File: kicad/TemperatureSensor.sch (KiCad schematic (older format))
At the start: 0 parts

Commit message: First draft of some of the sub-sheets
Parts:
- added R? (x3): 0Ω, symbol Device:R
- added U?: DS7505S, symbol FieldDevice_R2:DS7505S
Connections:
- new net: R?.1, U?.5 (A2)
- new net: R?.1, U?.6 (A1)
- new net: R?.1, U?.7 (A0)
- new net GND: R?.2, R?.2, R?.2, U?.4 (GND)
- new net O.S.: U?.3 (O.S.)
- new net SCL_TEMP: U?.2 (SCL)
- new net SDA: U?.1 (SDA)
- new net Vbb: U?.8 (VDD)
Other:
- note added: "Slave address is \n1 0 0 1 A2 A1 A0"
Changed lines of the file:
@@
 EESchema Schematic File Version 4
 LIBS:FieldDevice_R2-cache
+LIBS:FieldDevice_Power_5V-cache
 EELAYER 26 0
 EELAYER END
 $Descr A4 11693 8268
 encoding utf-8
-Sheet 1 8
+Sheet 4 8
 Title ""
 Date ""
@@
 Comment4 ""
 $EndDescr
+$Comp
+L FieldDevice_R2:DS7505S U?
+U 1 1 5C6AF879
+P 5750 3300
+F 0 "U?" H 6100 2950 50  0000 C CNN
+F 1 "DS7505S" H 5750 3300 50  0000 C CNN
+F 2 "" H 5800 3300 50  0001 C CNN
+F 3 "" H 5800 3300 50  0001 C CNN
+	1    5750 3300
+	1    0    0    -1
+$EndComp
+$Comp
+L FieldDevice_Power_5V-rescue:GND #PWR?
+U 1 1 5C6AF900
+P 5750 4100
+F 0 "#PWR?" H 5750 3850 50  0001 C CNN
+F 1 "GND" H 5755 3927 50  0000 C CNN
+F 2 "" H 5750 4100 50  0001 C CNN
+F 3 "" H 5750 4100 50  0001 C CNN
+	1    5750 4100
+	1    0    0    -1
+$EndComp
+Wire Wire Line
+	5750 3800 5750 4100
+$Comp
+L Device:R R?
+U 1 1 5C6AF92E
+P 6450 3650
+F 0 "R?" H 6520 3696 50  0000 L CNN
+F 1 "0Ω" H 6520 3605 50  0000 L CNN
+F 2 "" V 6380 3650 50  0001 C CNN
+F 3 "~" H 6450 3650 50  0001 C CNN
+	1    6450 3650
+	1    0    0    -1
+$EndComp
+$Comp
+L Device:R R?
+U 1 1 5C6AF9A1
+P 6700 3650
+F 0 "R?" H 6770 3696 50  0000 L CNN
+F 1 "0Ω" H 6770 3605 50  0000 L CNN
+F 2 "" V 6630 3650 50  0001 C CNN
+F 3 "~" H 6700 3650 50  0001 C CNN
+	1    6700 3650
+	1    0    0    -1
+$EndComp
+$Comp
+L Device:R R?
+U 1 1 5C6AF9C3
+P 6950 3650
+F 0 "R?" H 7020 3696 50  0000 L CNN
+F 1 "0Ω" H 7020 3605 50  0000 L CNN
+F 2 "" V 6880 3650 50  0001 C CNN
+F 3 "~" H 6950 3650 50  0001 C CNN
+	1    6950 3650
+	1    0    0    -1
+$EndComp
+Wire Wire Line
+	6350 3450 6450 3450
+Wire Wire Line
+	6450 3450 6450 3500
+Wire Wire Line
+	6350 3350 6700 3350
+Wire Wire Line
+	6700 3350 6700 3500
+Wire Wire Line
+	6350 3250 6950 3250
+Wire Wire Line
+	6950 3250 6950 3500
+$Comp
+L FieldDevice_Power_5V-rescue:GND #PWR?
+U 1 1 5C6AFAFC
+P 7050 4050
+F 0 "#PWR?" H 7050 3800 50  0001 C CNN
+F 1 "GND" H 7055 3877 50  0000 C CNN
+F 2 "" H 7050 4050 50  0001 C CNN
+F 3 "" H 7050 4050 50  0001 C CNN
+	1    7050 4050
+	1    0    0    -1
+$EndComp
+Text Notes 7050 3400 0    50   ~ 0
+Slave address is \n1 0 0 1 A2 A1 A0
+Wire Wire Line
+	6450 3800 6450 3950
+Wire Wire Line
+	6450 3950 6700 3950
+Wire Wire Line
+	7050 3950 7050 4050
+Wire Wire Line
+	6950 3800 6950 3950
+Connection ~ 6950 3950
+Wire Wire Line
+	6950 3950 7050 3950
+Wire Wire Line
+	6700 3800 6700 3950
+Connection ~ 6700 3950
+Wire Wire Line
+	6700 3950 6950 3950
+Wire Wire Line
+	5150 3100 4900 3100
+Wire Wire Line
+	5150 3200 4900 3200
+Wire Wire Line
+	5150 3450 4900 3450
+Text HLabel 4900 3450 0    50   Input ~ 0
+O.S.
+Text HLabel 4900 3200 0    50   Input ~ 0
+SCL_TEMP
+Text HLabel 4900 3100 0    50   Input ~ 0
+SDA
+Wire Wire Line
+	5750 2800 5750 2650
+Wire Wire Line
+	5750 2650 4900 2650
+Text HLabel 4900 2650 0    50   Input ~ 0
+Vbb
 $EndSCHEMATC

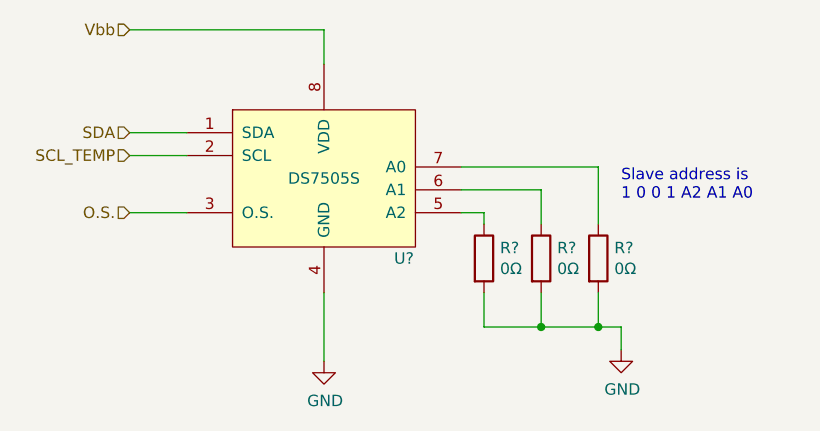
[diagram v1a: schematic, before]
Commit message: Added some more detail and moved the display from SPI to I2C
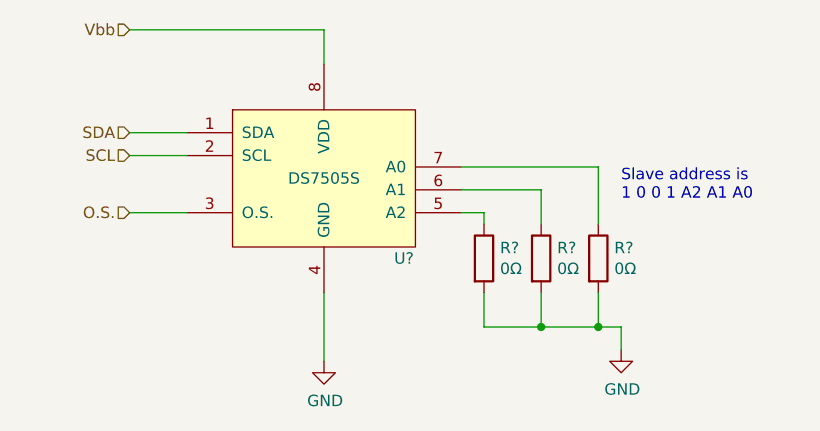
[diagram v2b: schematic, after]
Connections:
- net SCL_TEMP renamed SCL
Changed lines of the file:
@@
 EESchema Schematic File Version 4
 LIBS:FieldDevice_R2-cache
-LIBS:FieldDevice_Power_5V-cache
-EELAYER 26 0
+EELAYER 29 0
 EELAYER END
 $Descr A4 11693 8268
@@
 O.S.
 Text HLabel 4900 3200 0    50   Input ~ 0
-SCL_TEMP
+SCL
 Text HLabel 4900 3100 0    50   Input ~ 0
 SDA
